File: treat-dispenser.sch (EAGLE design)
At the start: 40 parts, among them U1 MCP73831, U2 TPS6103x, U3 ATMEGA32U4, Y1 16MHz

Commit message: fixed part names
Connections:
- net D10: no longer JP3.RIGHT
- net D2: now also JP3.LEFT, JP3.RIGHT
- net D3: now also JP4.LEFT, JP4.RIGHT
- net D6: no longer JP4.LEFT
- net D8: no longer JP4.RIGHT
- net D9: no longer JP3.LEFT
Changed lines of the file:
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@@
 <grid distance="0.1" unitdist="inch" unit="inch" style="lines" multiple="1" display="no" altdistance="0.01" altunitdist="inch" altunit="inch"/>
 <layers>
-<layer number="1" name="Top" color="4" fill="1" visible="yes" active="no"/>
-<layer number="16" name="Bottom" color="1" fill="1" visible="yes" active="no"/>
-<layer number="17" name="Pads" color="2" fill="1" visible="yes" active="no"/>
-<layer number="18" name="Vias" color="2" fill="1" visible="yes" active="no"/>
-<layer number="19" name="Unrouted" color="6" fill="1" visible="yes" active="no"/>
-<layer number="20" name="Dimension" color="15" fill="1" visible="yes" active="no"/>
-<layer number="21" name="tPlace" color="14" fill="1" visible="yes" active="no"/>
-<layer number="22" name="bPlace" color="14" fill="1" visible="yes" active="no"/>
-<layer number="23" name="tOrigins" color="15" fill="1" visible="yes" active="no"/>
-<layer number="24" name="bOrigins" color="15" fill="1" visible="yes" active="no"/>
-<layer number="25" name="tNames" color="7" fill="1" visible="yes" active="no"/>
-<layer number="26" name="bNames" color="7" fill="1" visible="yes" active="no"/>
-<layer number="27" name="tValues" color="7" fill="1" visible="yes" active="no"/>
-<layer number="28" name="bValues" color="7" fill="1" visible="yes" active="no"/>
+<layer number="1" name="Top" color="4" fill="1" visible="no" active="no"/>
+<layer number="16" name="Bottom" color="1" fill="1" visible="no" active="no"/>
+<layer number="17" name="Pads" color="2" fill="1" visible="no" active="no"/>
+<layer number="18" name="Vias" color="2" fill="1" visible="no" active="no"/>
+<layer number="19" name="Unrouted" color="6" fill="1" visible="no" active="no"/>
+<layer number="20" name="Dimension" color="15" fill="1" visible="no" active="no"/>
+<layer number="21" name="tPlace" color="14" fill="1" visible="no" active="no"/>
+<layer number="22" name="bPlace" color="14" fill="1" visible="no" active="no"/>
+<layer number="23" name="tOrigins" color="15" fill="1" visible="no" active="no"/>
+<layer number="24" name="bOrigins" color="15" fill="1" visible="no" active="no"/>
+<layer number="25" name="tNames" color="7" fill="1" visible="no" active="no"/>
+<layer number="26" name="bNames" color="7" fill="1" visible="no" active="no"/>
+<layer number="27" name="tValues" color="7" fill="1" visible="no" active="no"/>
+<layer number="28" name="bValues" color="7" fill="1" visible="no" active="no"/>
 <layer number="29" name="tStop" color="7" fill="3" visible="no" active="no"/>
 <layer number="30" name="bStop" color="7" fill="6" visible="no" active="no"/>
@@
 <layer number="35" name="tGlue" color="7" fill="4" visible="no" active="no"/>
 <layer number="36" name="bGlue" color="7" fill="5" visible="no" active="no"/>
-<layer number="37" name="tTest" color="7" fill="1" visible="yes" active="no"/>
-<layer number="38" name="bTest" color="7" fill="1" visible="yes" active="no"/>
+<layer number="37" name="tTest" color="7" fill="1" visible="no" active="no"/>
+<layer number="38" name="bTest" color="7" fill="1" visible="no" active="no"/>
 <layer number="39" name="tKeepout" color="4" fill="11" visible="no" active="no"/>
 <layer number="40" name="bKeepout" color="1" fill="11" visible="no" active="no"/>
@@
 <layer number="44" name="Drills" color="7" fill="1" visible="no" active="no"/>
 <layer number="45" name="Holes" color="7" fill="1" visible="no" active="no"/>
-<layer number="46" name="Milling" color="3" fill="1" visible="yes" active="no"/>
-<layer number="47" name="Measures" color="7" fill="1" visible="yes" active="no"/>
-<layer number="48" name="Document" color="7" fill="1" visible="yes" active="no"/>
-<layer number="49" name="Reference" color="7" fill="1" visible="yes" active="no"/>
-<layer number="50" name="dxf" color="7" fill="1" visible="yes" active="no"/>
-<layer number="51" name="tDocu" color="7" fill="1" visible="yes" active="no"/>
-<layer number="52" name="bDocu" color="7" fill="1" visible="yes" active="no"/>
-<layer number="53" name="tGND_GNDA" color="7" fill="9" visible="yes" active="no"/>
-<layer number="54" name="bGND_GNDA" color="1" fill="9" visible="yes" active="no"/>
-<layer number="56" name="wert" color="7" fill="1" visible="yes" active="no"/>
-<layer number="57" name="tCAD" color="7" fill="1" visible="yes" active="no"/>
-<layer number="59" name="tCarbon" color="7" fill="1" visible="yes" active="no"/>
-<layer number="60" name="bCarbon" color="7" fill="1" visible="yes" active="no"/>
+<layer number="46" name="Milling" color="3" fill="1" visible="no" active="no"/>
+<layer number="47" name="Measures" color="7" fill="1" visible="no" active="no"/>
+<layer number="48" name="Document" color="7" fill="1" visible="no" active="no"/>
+<layer number="49" name="Reference" color="7" fill="1" visible="no" active="no"/>
+<layer number="50" name="dxf" color="7" fill="1" visible="no" active="no"/>
+<layer number="51" name="tDocu" color="7" fill="1" visible="no" active="no"/>
+<layer number="52" name="bDocu" color="7" fill="1" visible="no" active="no"/>
+<layer number="53" name="tGND_GNDA" color="7" fill="9" visible="no" active="no"/>
+<layer number="54" name="bGND_GNDA" color="1" fill="9" visible="no" active="no"/>
+<layer number="56" name="wert" color="7" fill="1" visible="no" active="no"/>
+<layer number="57" name="tCAD" color="7" fill="1" visible="no" active="no"/>
+<layer number="59" name="tCarbon" color="7" fill="1" visible="no" active="no"/>
+<layer number="60" name="bCarbon" color="7" fill="1" visible="no" active="no"/>
 <layer number="90" name="Modules" color="5" fill="1" visible="yes" active="yes"/>
 <layer number="91" name="Nets" color="2" fill="1" visible="yes" active="yes"/>
@@
 <pinref part="U3" gate="G$1" pin="PB5(ADC12)"/>
 </segment>
-<segment>
-<pinref part="JP3" gate="G$1" pin="LEFT"/>
-<wire x1="17.78" y1="147.32" x2="25.4" y2="147.32" width="0.1524" layer="91"/>
-<label x="20.32" y="147.32" size="1.778" layer="95"/>
-</segment>
 </net>
 <net name="D8" class="0">
@@
 <label x="114.3" y="104.14" size="1.778" layer="95"/>
 <pinref part="U3" gate="G$1" pin="PB4(ADC11)"/>
-</segment>
-<segment>
-<pinref part="JP4" gate="G$1" pin="RIGHT"/>
-<wire x1="17.78" y1="127" x2="25.4" y2="127" width="0.1524" layer="91"/>
-<label x="20.32" y="127" size="1.778" layer="95"/>
 </segment>
 </net>
@@
 <pinref part="U3" gate="G$1" pin="PD1(SDA)"/>
 </segment>
+<segment>
+<pinref part="JP3" gate="G$1" pin="LEFT"/>
+<wire x1="17.78" y1="147.32" x2="25.4" y2="147.32" width="0.1524" layer="91"/>
+<label x="20.32" y="147.32" size="1.778" layer="95"/>
+</segment>
+<segment>
+<pinref part="JP3" gate="G$1" pin="RIGHT"/>
+<wire x1="17.78" y1="144.78" x2="25.4" y2="144.78" width="0.1524" layer="91"/>
+<label x="20.32" y="144.78" size="1.778" layer="95"/>
+</segment>
 </net>
 <net name="D3" class="0">
@@
 <pinref part="U3" gate="G$1" pin="PD0(SCL)"/>
 </segment>
+<segment>
+<pinref part="JP4" gate="G$1" pin="LEFT"/>
+<wire x1="17.78" y1="129.54" x2="25.4" y2="129.54" width="0.1524" layer="91"/>
+<label x="20.32" y="129.54" size="1.778" layer="95"/>
+</segment>
+<segment>
+<pinref part="JP4" gate="G$1" pin="RIGHT"/>
+<wire x1="17.78" y1="127" x2="25.4" y2="127" width="0.1524" layer="91"/>
+<label x="20.32" y="127" size="1.778" layer="95"/>
+</segment>
 </net>
 <net name="D4" class="0">
@@
 <pinref part="U3" gate="G$1" pin="PD7(ADC10)"/>
 </segment>
-<segment>
-<pinref part="JP4" gate="G$1" pin="LEFT"/>
-<wire x1="17.78" y1="129.54" x2="25.4" y2="129.54" width="0.1524" layer="91"/>
-<label x="20.32" y="129.54" size="1.778" layer="95"/>
-</segment>
 </net>
 <net name="D7" class="0">
@@
 <pinref part="U3" gate="G$1" pin="PB6(ADC13)"/>
 </segment>
-<segment>
-<pinref part="JP3" gate="G$1" pin="RIGHT"/>
-<wire x1="17.78" y1="144.78" x2="25.4" y2="144.78" width="0.1524" layer="91"/>
-<label x="20.32" y="144.78" size="1.778" layer="95"/>
-</segment>
-</net>
+</net>

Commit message: rev A initial commit
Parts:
- removed D1: Yellow, SparkFun:LED0603
- removed D3: Green, SparkFun:LED0603
- removed D4: red, SparkFun:LED0603
- removed FRAME1: FRAME-LETTER, SparkFun-Aesthetics:FRAME-LETTER
- removed JP4: (no value), SparkFun-Connectors:AUDIO-JACKPTH
- removed JP8: (no value), SparkFun-Connectors:M03PTH
- removed R4, R6, R9: 470, SparkFun:RESISTOR0603-RES
- removed U3: ATMEGA32U4, Testing:ATMEGA32U4OUTFAKES
- added U$1: ATMEGA32U4TQFP-44, SparkFun-DigitalIC:ATMEGA32U4TQFP-44
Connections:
- removed net N$5: D1.C, R4.2
- removed net N$7: D3.C, R6.2
- removed net STAT: R9.1, U1.STAT
- removed net TXLED: R6.1, U3.PD5
- net A0: now also U$1.PF7(ADC7); no longer JP8.3, U3.PF7(ADC7)
- net A1: now also U$1.PF6(ADC6); no longer U3.PF6(ADC6)
- net A2: now also U$1.PF5(ADC5); no longer U3.PF5(ADC5)
- net A3: now also U$1.PF4(ADC4); no longer U3.PF4(ADC4)
- net A4: now also U$1.PF1(ADC1); no longer U3.PF1(ADC1)
- net A5: now also U$1.PF0(ADC0); no longer U3.PF0(ADC0)
- net AREF: now also U$1.AREF; no longer U3.AREF
- net D10: now also U$1.PB6(ADC13); no longer U3.PB6(ADC13)
- net D11: now also U$1.PB7; no longer U3.PB7
- net D12: now also U$1.PD6(ADC9); no longer U3.PD6(ADC9)
- net D13: now also U$1.PC7; no longer U3.PC7
- net D14: now also U$1.PB0(SS); no longer R4.1, U3.PB3(MISO)
- net D2: now also U$1.PD1(SDA); no longer JP3.RIGHT, U3.PD1(SDA)
- net D3: now also JP3.RIGHT, U$1.PD0(SCL); no longer JP4.LEFT, JP4.RIGHT, U3.PD0(SCL)
- net D4: now also U$1.PD4(ADC8), U1.STAT; no longer U3.PD4(ADC8)
- net D5: now also U$1.PC6; no longer U3.PC6
- net D6: now also U$1.PD7(ADC10); no longer U3.PD7(ADC10)
- net D7: now also U$1.PE6; no longer U3.PE6
- net D8: now also U$1.PB4(ADC11); no longer U3.PB4(ADC11)
- net D9: now also U$1.PB5(ADC12); no longer U3.PB5(ADC12)
- net GND: now also U$1.GND@15, U$1.GND@23, U$1.GND@35, U$1.GND@43, U$1.PE2/!HWB, U$1.UGND; no longer JP4.SLEEVE, JP8.1, U3.GND@15, U3.GND@23, U3.GND@35, U3.GND@43, U3.PE2/!HWB, U3.UGND
- net MISO: now also U$1.PB3(MISO); no longer U3.PB0(SS)
- net MOSI: now also U$1.PB2(MOSI); no longer U3.PB2(MOSI)
- net N$1: now also U$1.XTAL2; no longer U3.XTAL2
- net N$2: now also U$1.XTAL1; no longer U3.XTAL1
- net N$3: now also U$1.PD5; no longer D4.C, R9.2
- net N$4: now also U$1.UCAP; no longer U3.UCAP
- net RD+: now also U$1.D+; no longer U3.D+
- net RD-: now also U$1.D-; no longer U3.D-
- net RESET: now also U$1.!RESET; no longer U3.!RESET
- net RXI: now also U$1.PD2(RX); no longer U3.PD2(RX)
- net SCK: now also U$1.PB1(SCK); no longer U3.PB1(SCK)
- net TXO: now also U$1.PD3(TX); no longer U3.PD3(TX)
- net UVCC: now also U$1.UVCC, U$1.VBUS; no longer D4.A, U3.UVCC, U3.VBUS
- net VCC: now also U$1.AVCC@24, U$1.AVCC@44, U$1.VCC@14, U$1.VCC@34; no longer D1.A, D3.A, JP8.2, U3.AVCC@24, U3.AVCC@44, U3.VCC@14, U3.VCC@34
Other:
- moved on the sheet: C9

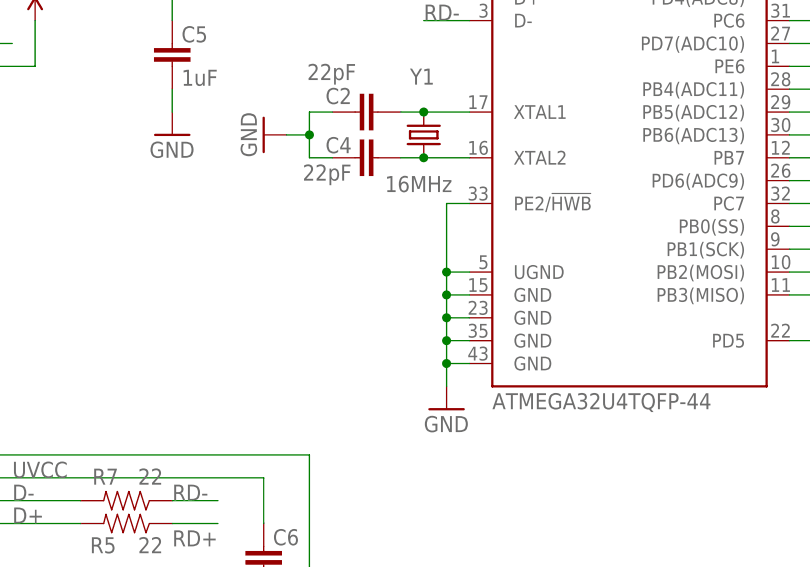
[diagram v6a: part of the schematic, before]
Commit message: rev A update with new board dxf
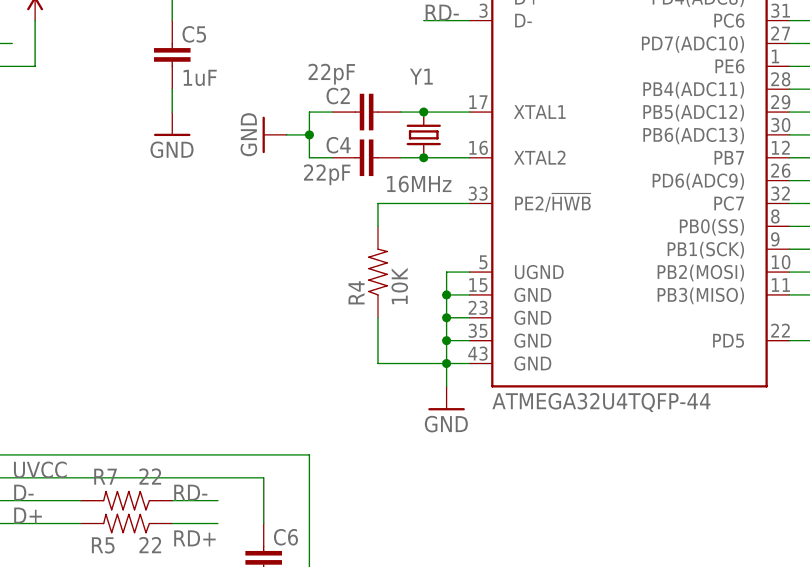
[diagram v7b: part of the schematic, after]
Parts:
- added R4: 10K, SparkFun:RESISTOR0603-RES
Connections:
- new net N$5: R4.2, U$1.PE2/!HWB
- net GND: now also R4.1; no longer U$1.PE2/!HWB
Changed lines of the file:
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@@
 <grid distance="0.1" unitdist="inch" unit="inch" style="lines" multiple="1" display="no" altdistance="0.01" altunitdist="inch" altunit="inch"/>
 <layers>
-<layer number="1" name="Top" color="4" fill="1" visible="yes" active="no"/>
-<layer number="16" name="Bottom" color="1" fill="1" visible="yes" active="no"/>
-<layer number="17" name="Pads" color="2" fill="1" visible="yes" active="no"/>
-<layer number="18" name="Vias" color="2" fill="1" visible="yes" active="no"/>
-<layer number="19" name="Unrouted" color="6" fill="1" visible="yes" active="no"/>
-<layer number="20" name="Dimension" color="15" fill="1" visible="yes" active="no"/>
-<layer number="21" name="tPlace" color="14" fill="1" visible="yes" active="no"/>
-<layer number="22" name="bPlace" color="14" fill="1" visible="yes" active="no"/>
-<layer number="23" name="tOrigins" color="15" fill="1" visible="yes" active="no"/>
-<layer number="24" name="bOrigins" color="15" fill="1" visible="yes" active="no"/>
-<layer number="25" name="tNames" color="7" fill="1" visible="yes" active="no"/>
-<layer number="26" name="bNames" color="7" fill="1" visible="yes" active="no"/>
-<layer number="27" name="tValues" color="7" fill="1" visible="yes" active="no"/>
-<layer number="28" name="bValues" color="7" fill="1" visible="yes" active="no"/>
+<layer number="1" name="Top" color="4" fill="1" visible="no" active="no"/>
+<layer number="16" name="Bottom" color="1" fill="1" visible="no" active="no"/>
+<layer number="17" name="Pads" color="2" fill="1" visible="no" active="no"/>
+<layer number="18" name="Vias" color="2" fill="1" visible="no" active="no"/>
+<layer number="19" name="Unrouted" color="6" fill="1" visible="no" active="no"/>
+<layer number="20" name="Dimension" color="15" fill="1" visible="no" active="no"/>
+<layer number="21" name="tPlace" color="14" fill="1" visible="no" active="no"/>
+<layer number="22" name="bPlace" color="14" fill="1" visible="no" active="no"/>
+<layer number="23" name="tOrigins" color="15" fill="1" visible="no" active="no"/>
+<layer number="24" name="bOrigins" color="15" fill="1" visible="no" active="no"/>
+<layer number="25" name="tNames" color="7" fill="1" visible="no" active="no"/>
+<layer number="26" name="bNames" color="7" fill="1" visible="no" active="no"/>
+<layer number="27" name="tValues" color="7" fill="1" visible="no" active="no"/>
+<layer number="28" name="bValues" color="7" fill="1" visible="no" active="no"/>
 <layer number="29" name="tStop" color="7" fill="3" visible="no" active="no"/>
 <layer number="30" name="bStop" color="7" fill="6" visible="no" active="no"/>
@@
 <layer number="35" name="tGlue" color="7" fill="4" visible="no" active="no"/>
 <layer number="36" name="bGlue" color="7" fill="5" visible="no" active="no"/>
-<layer number="37" name="tTest" color="7" fill="1" visible="yes" active="no"/>
-<layer number="38" name="bTest" color="7" fill="1" visible="yes" active="no"/>
+<layer number="37" name="tTest" color="7" fill="1" visible="no" active="no"/>
+<layer number="38" name="bTest" color="7" fill="1" visible="no" active="no"/>
 <layer number="39" name="tKeepout" color="4" fill="11" visible="no" active="no"/>
 <layer number="40" name="bKeepout" color="1" fill="11" visible="no" active="no"/>
@@
 <layer number="44" name="Drills" color="7" fill="1" visible="no" active="no"/>
 <layer number="45" name="Holes" color="7" fill="1" visible="no" active="no"/>
-<layer number="46" name="Milling" color="3" fill="1" visible="yes" active="no"/>
-<layer number="47" name="Measures" color="7" fill="1" visible="yes" active="no"/>
-<layer number="48" name="Document" color="7" fill="1" visible="yes" active="no"/>
-<layer number="49" name="Reference" color="7" fill="1" visible="yes" active="no"/>
-<layer number="50" name="dxf" color="7" fill="1" visible="yes" active="no"/>
-<layer number="51" name="tDocu" color="7" fill="1" visible="yes" active="no"/>
-<layer number="52" name="bDocu" color="7" fill="1" visible="yes" active="no"/>
-<layer number="53" name="tGND_GNDA" color="7" fill="9" visible="yes" active="no"/>
-<layer number="54" name="bGND_GNDA" color="1" fill="9" visible="yes" active="no"/>
-<layer number="56" name="wert" color="7" fill="1" visible="yes" active="no"/>
-<layer number="57" name="tCAD" color="7" fill="1" visible="yes" active="no"/>
-<layer number="59" name="tCarbon" color="7" fill="1" visible="yes" active="no"/>
-<layer number="60" name="bCarbon" color="7" fill="1" visible="yes" active="no"/>
+<layer number="46" name="Milling" color="3" fill="1" visible="no" active="no"/>
+<layer number="47" name="Measures" color="7" fill="1" visible="no" active="no"/>
+<layer number="48" name="Document" color="7" fill="1" visible="no" active="no"/>
+<layer number="49" name="Reference" color="7" fill="1" visible="no" active="no"/>
+<layer number="50" name="dxf" color="7" fill="1" visible="no" active="no"/>
+<layer number="51" name="tDocu" color="7" fill="1" visible="no" active="no"/>
+<layer number="52" name="bDocu" color="7" fill="1" visible="no" active="no"/>
+<layer number="53" name="tGND_GNDA" color="7" fill="9" visible="no" active="no"/>
+<layer number="54" name="bGND_GNDA" color="1" fill="9" visible="no" active="no"/>
+<layer number="56" name="wert" color="7" fill="1" visible="no" active="no"/>
+<layer number="57" name="tCAD" color="7" fill="1" visible="no" active="no"/>
+<layer number="59" name="tCarbon" color="7" fill="1" visible="no" active="no"/>
+<layer number="60" name="bCarbon" color="7" fill="1" visible="no" active="no"/>
 <layer number="90" name="Modules" color="5" fill="1" visible="yes" active="yes"/>
 <layer number="91" name="Nets" color="2" fill="1" visible="yes" active="yes"/>
@@
 </part>
 <part name="U$1" library="SparkFun-DigitalIC" deviceset="ATMEGA32U4" device="TQFP-44"/>
+<part name="R4" library="SparkFun" deviceset="RESISTOR" device="0603-RES" value="10K">
+<attribute name="PN" value="CR0603-JW-103ELF"/>
+</part>
 </parts>
 <sheets>
@@
 </instance>
 <instance part="U$1" gate="G$1" x="93.98" y="111.76"/>
+<instance part="R4" gate="G$1" x="66.04" y="83.82" rot="R90">
+<attribute name="PN" x="66.04" y="83.82" size="1.778" layer="96" rot="R90" display="off"/>
+</instance>
 </instances>
 <busses>
@@
 <wire x1="76.2" y1="83.82" x2="73.66" y2="83.82" width="0.1524" layer="91"/>
 <wire x1="73.66" y1="83.82" x2="73.66" y2="81.28" width="0.1524" layer="91"/>
-<wire x1="76.2" y1="91.44" x2="73.66" y2="91.44" width="0.1524" layer="91"/>
-<wire x1="73.66" y1="91.44" x2="73.66" y2="83.82" width="0.1524" layer="91"/>
 <junction x="73.66" y="73.66"/>
 <junction x="73.66" y="76.2"/>
 <junction x="73.66" y="78.74"/>
 <junction x="73.66" y="81.28"/>
-<junction x="73.66" y="83.82"/>
 <pinref part="GND2" gate="1" pin="GND"/>
 <pinref part="U$1" gate="G$1" pin="GND@15"/>
@@
 <pinref part="U$1" gate="G$1" pin="GND@35"/>
 <pinref part="U$1" gate="G$1" pin="GND@43"/>
-<pinref part="U$1" gate="G$1" pin="PE2/!HWB"/>
 <pinref part="U$1" gate="G$1" pin="UGND"/>
+<pinref part="R4" gate="G$1" pin="1"/>
+<wire x1="66.04" y1="78.74" x2="66.04" y2="73.66" width="0.1524" layer="91"/>
+<wire x1="66.04" y1="73.66" x2="73.66" y2="73.66" width="0.1524" layer="91"/>
 </segment>
 <segment>
@@
 </segment>
 </net>
+<net name="N$5" class="1">
+<segment>
+<pinref part="U$1" gate="G$1" pin="PE2/!HWB"/>
+<pinref part="R4" gate="G$1" pin="2"/>
+<wire x1="76.2" y1="91.44" x2="66.04" y2="91.44" width="0.1524" layer="91"/>
+<wire x1="66.04" y1="91.44" x2="66.04" y2="88.9" width="0.1524" layer="91"/>
+</segment>
+</net>

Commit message: mfg files update
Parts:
- U$1: PN (none) -> ATMEGA32U4-AUR
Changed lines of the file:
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@@
 <attribute name="PN" value="SRP4020TA-6R8M"/>
 </part>
-<part name="U$1" library="SparkFun-DigitalIC" deviceset="ATMEGA32U4" device="TQFP-44"/>
+<part name="U$1" library="SparkFun-DigitalIC" deviceset="ATMEGA32U4" device="TQFP-44">
+<attribute name="PN" value="ATMEGA32U4-AUR"/>
+</part>
 <part name="R4" library="SparkFun" deviceset="RESISTOR" device="0603-RES" value="10K">
 <attribute name="PN" value="CR0603-JW-103ELF"/>
@@
 <attribute name="PN" x="157.48" y="101.6" size="1.778" layer="96" rot="R90" display="off"/>
 </instance>
-<instance part="U$1" gate="G$1" x="93.98" y="111.76"/>
+<instance part="U$1" gate="G$1" x="93.98" y="111.76">
+<attribute name="PN" x="93.98" y="111.76" size="1.778" layer="96" display="off"/>
+</instance>
 <instance part="R4" gate="G$1" x="66.04" y="83.82" rot="R90">
 <attribute name="PN" x="66.04" y="83.82" size="1.778" layer="96" rot="R90" display="off"/>
